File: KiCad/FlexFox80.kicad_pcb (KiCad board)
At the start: 4 copper layers, 111.2 x 80 mm, 169 parts, among them J101 DIN-5_180degree, J102 Conn_01x02, J203 V4, J301 DB9_Female, J302 Conn_01x06, J303 DB9_Male, P203 Power Pole, P301 ISP/PDI, P302 Thru, P304 Header, Q101 LMN200B02, Q102 IRF610, Q201 MUN5213DW1, Q202 DMP4025LSD, Q203 RJK0354DSP, Q301 PN2222A, SW301 SPST, U107 LM5134B, U201 DAC081C085, U202 OPA171, U203 LTC3600, U204 MIC2196, U301 DS3231, U302 ATmega1284P-AU, U303 LP2992, U304 SI5351A, U305 74HC1G08, U306 LP2992, U307 SN74CB3Q3305, U308 LP2992, X301 ASTX-H11-25.MHZ, Y301 20 MHz

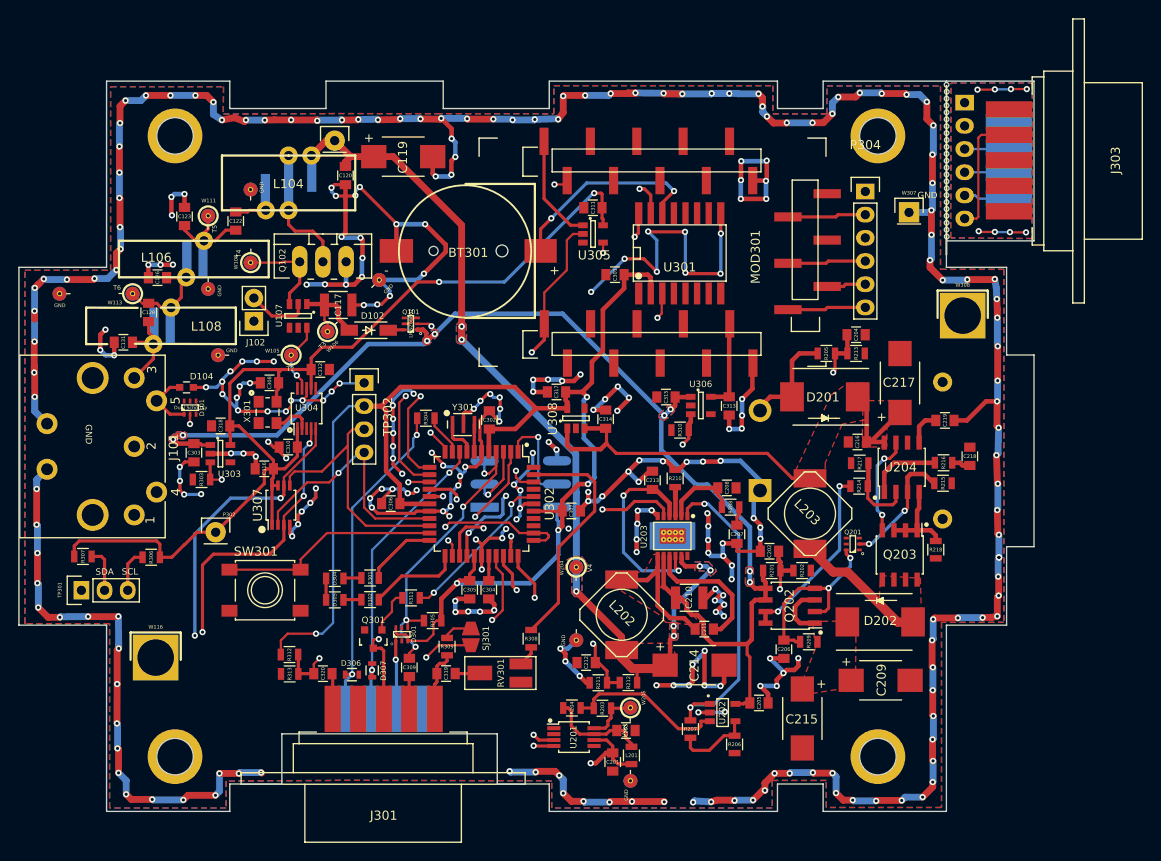
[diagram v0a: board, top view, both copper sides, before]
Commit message: Updates for AVR128DA48
o Board changes
o Gerbers updated
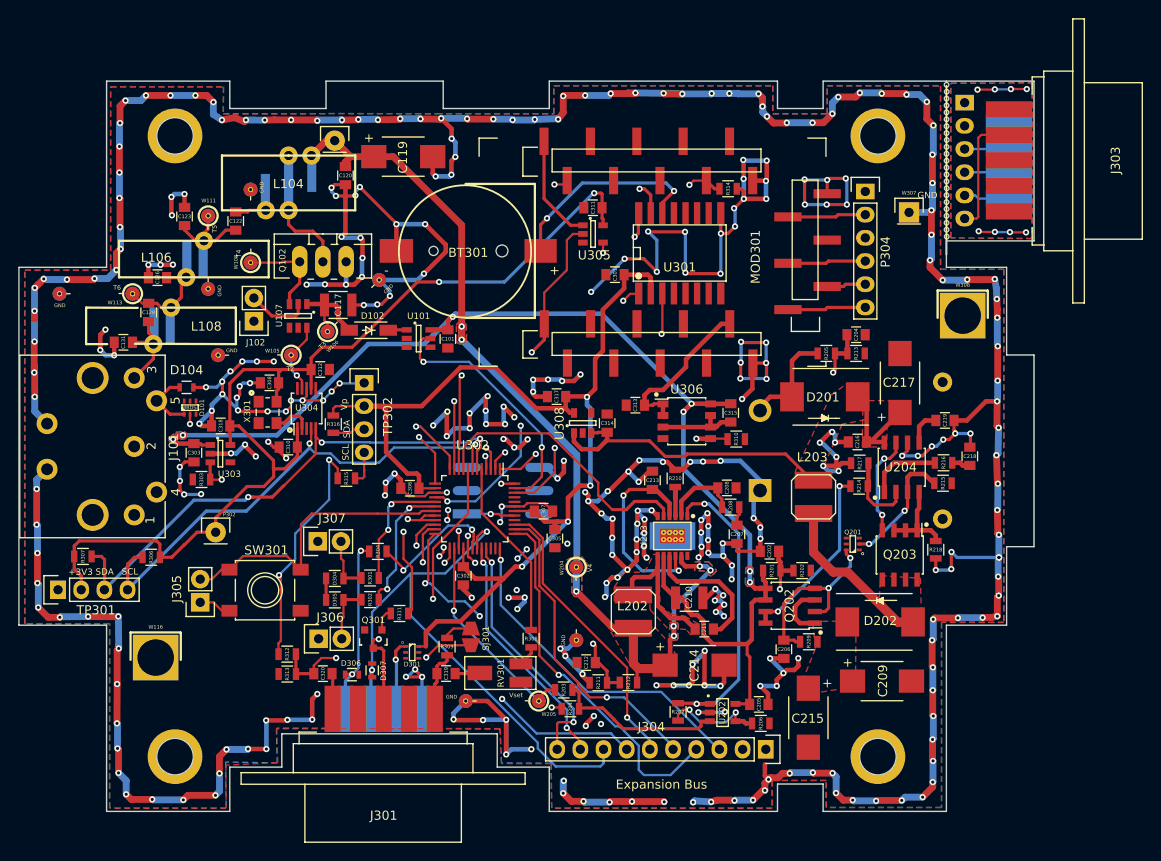
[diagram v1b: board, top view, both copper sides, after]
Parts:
- removed C201, C203, C304: 10uF, Capacitors_SMD:C_0805
- removed C309, C316: 100nF, Capacitors_SMD:C_0805
- removed L201: 10uH, Resistors_SMD:R_0805
- removed Q101: LMN200B02, TO_SOT_Packages_SMD:SOT-363-0.65
- removed R305: 10k, Resistors_SMD:R_0805
- removed U201: DAC081C085, Housings_SSOP:MSOP-8_3x3mm_Pitch0.65mm
- removed U307: SN74CB3Q3305, Housings_SSOP:TSSOP-8_3x3mm_Pitch0.65mm
- removed Y301: 20 MHz, Crystals:CSTNE20M0V53Z000R0
- added C101: 10uF, Capacitors_SMD:C_0805, F.Cu at (63.2, 58.2)
- added J304: Conn_01x10, Pin_Headers:Pin_Header_Straight_1x10, F.Cu at (98.0, 103.2)
- added J305: Conn_01x02, Pin_Headers:Pin_Header_Straight_1x02, F.Cu at (36.1, 87.1)
- added J306: Conn_01x02, Pin_Headers:Pin_Header_Straight_1x02, F.Cu at (49.0, 91.1)
- added J307: Conn_01x02, Pin_Headers:Pin_Header_Straight_1x02, F.Cu at (48.9, 80.4)
- added R314: 560k, Resistors_SMD:R_0805, F.Cu at (93.9, 41.8)
- added R315: 10k, Resistors_SMD:R_0805, F.Cu at (52.1, 73.5)
- added R316: 10k, Resistors_SMD:R_0805, F.Cu at (50.6, 67.6)
- added U101: TPS22810DBVT, TO_SOT_Packages_SMD:SOT-23-6, F.Cu at (60.0, 58.2)
- D101: value Dual Schottky -> MBD54
- D104: value 5V -> ESD; footprint Capacitors_SMD:C_0603 -> Resistors_SMD:R_0603
- D301: value MBD54DWT1GOSCT-ND -> MBD54
- L202, L203: footprint Inductors:CDR7D28MN -> Inductors:2020
- R204: value 536k -> 392k
- R206: value 46.4k -> 27k
- TP301: footprint Pin_Headers:Pin_Header_Straight_1x03 -> Pin_Headers:Pin_Header_Straight_1x04
- U302: value ATmega1284P-AU -> AVR128DA48; footprint Housings_QFP:TQFP-44_10x10mm_Pitch0.8mm -> Housings_QFP:TQFP-48_7x7mm_Pitch0.5mm
- U303, U308: value LP2992 -> LD2985BM33R
- U306: value LP2992 -> LT1763CS8-5; footprint TO_SOT_Packages_SMD:SOT-23-5 -> Housings_SOIC:SOIC-8_3.9x4.9mm_Pitch1.27mm
- X301: value ASTX-H11-25.MHZ -> 25.MHZ TCXO
- moved C302 17.3 mm to (64.9, 84.2), turned to 90 degrees
- moved R304 15.5 mm to (55.5, 81.5)
- moved C305 10.9 mm to (74.9, 80.1)
- moved C313 10.3 mm to (83.7, 65.5), turned to 0 degrees
- moved W205 10.1 mm to (73.2, 97.9), turned to 180 degrees
- moved C315 7.31 mm to (94.2, 66.3), turned to 90 degrees
- moved R310 6.23 mm to (94.8, 69.2), turned to 0 degrees
- moved R203 4.69 mm to (75.9, 96.7), turned to 180 degrees
- moved R206 3.68 mm to (97.5, 100.4), turned to 0 degrees
- moved C307 3.05 mm to (73.7, 77.1)
- moved C306 2.69 mm to (59.0, 74.6)
- moved TP301 2.56 mm to (20.5, 85.7)
- moved U306 2.32 mm to (89.4, 67.3)
- moved R207 2.31 mm to (88.4, 99.1)
- moved D301 2.28 mm to (59.3, 92.6), turned to 270 degrees
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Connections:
- net /Digital/RXD1 renamed WIFI_TX
- D301 pad 3: Vproc -> (no net)
- D301 pad 4: ~RESET~ -> (no net)
- MOD301 pad 13: Net-(MOD301-Pad13) -> /Digital/ADC7
- MOD301 pad 19: DI_TXD0 -> WIFI_RX
- P301 pad 1: MISO -> Net-(P301-Pad1)
- P301 pad 3: SCK -> Net-(P301-Pad3)
- P301 pad 4: MOSI -> Net-(P301-Pad4)
- P301 pad 5: ~RESET~ -> Net-(P301-Pad5)
- R203 pad 2: Net-(R203-Pad2) -> DAC_OUTPUT
- R204 pad 1: Net-(C203-Pad2) -> +3V3_L8
- R301 pad 2: /Digital/PC3 -> /Digital/PC5
- R302 pad 2: /Digital/PC4 -> /Digital/PC6
- R304 pad 1: /Digital/TXD0 -> /Digital/TXD4
- R306 pad 2: DI_SCL -> /Digital/SCL1
- R307 pad 2: DI_SDA -> /Digital/SDA1
- SW301 pad 1: /Digital/PC2 -> /Digital/PC7
- TP301 pad 2: DI_SDA -> +3V3_L8
- TP301 pad 3: DI_SCL -> /Digital/SDA1
- U301 pad 1: Net-(U301-Pad1) -> 32KHZ_SQUAREWAVE
- U302 pad 1: MOSI -> WIFI_ENABLE
- U302 pad 10: /Digital/TXD0 -> WIFI_RX
- U302 pad 12: DI_TXD0 -> RTC_SDA
- U302 pad 13: HF_ENABLE -> RTC_SCL
- U302 pad 14: 3V3_PWR_ENABLE -> Vproc
- U302 pad 15: MAIN_PWR_ENABLE -> GND
- U302 pad 16: TX_FINAL_VOLTAGE_ENABLE -> 32KHZ_SQUAREWAVE
- U302 pad 17: Vproc -> /Digital/PC5
- U302 pad 18: GND -> /Digital/PC6
- U302 pad 19: RTC_SCL -> /Digital/PC7
- U302 pad 2: MISO -> ~WIFI_RESET~
- U302 pad 20: RTC_SDA -> 80M_ANTENNA_DETECT
- U302 pad 21: /Digital/PC2 -> 80M_ANTENNA_DETECT
- U302 pad 22: /Digital/PC3 -> PROC_HT_AUDIO_IN
- U302 pad 23: /Digital/PC4 -> TX_BATTERY_VOLTAGE
- U302 pad 24: ~ANT_CONNECT_INT~ -> TX_+12_VOLTAGE
- U302 pad 25: WIFI_ENABLE -> TX_PA_VOLTAGE
- U302 pad 26: ~WIFI_RESET~ -> DAC_OUTPUT
- U302 pad 27: Vproc -> /Digital/ADC7
- U302 pad 28: GND -> Vproc
- U302 pad 29: Net-(C304-Pad2) -> GND
- U302 pad 3: SCK -> 3V3_PWR_ENABLE
- U302 pad 30: PROC_HT_AUDIO_IN -> /Digital/TXD4
- U302 pad 31: TX_PA_VOLTAGE -> RXD_TO_FTDI
- U302 pad 32: TX_BATTERY_VOLTAGE -> /Digital/PE2
- U302 pad 33: TX_+12_VOLTAGE -> /Digital/PE3
- U302 pad 34: 80M_ANTENNA_DETECT -> Net-(U302-Pad34)
- U302 pad 35: 80M_ANTENNA_DETECT -> Net-(U302-Pad35)
- U302 pad 36: /Digital/PA1 -> /Digital/PF2
- U302 pad 37: /Digital/PA0 -> /Digital/PF3
- U302 pad 38: Vproc -> /Digital/PF4
- U302 pad 39: GND -> /Digital/PF5
- U302 pad 4: ~RESET~ -> PROC_PTT_OUT
- U302 pad 40: PROC_PTT_OUT -> /Digital/PF6
- U302 pad 41: /Digital/PB1 -> Net-(P301-Pad1)
- U302 pad 42: RTC_SQW -> Vproc
- U302 pad 43: PROC_TONE_OUT -> GND
- U302 pad 44: /Digital/PB4 -> /Digital/PA0
- U302 pad 5: Vproc -> PROC_TONE_OUT
- U302 pad 6: GND -> /Digital/SDA1
- U302 pad 7: Net-(U302-Pad7) -> /Digital/SCL1
- U302 pad 8: Net-(U302-Pad8) -> MAIN_PWR_ENABLE
- U302 pad 9: RXD_TO_FTDI -> TX_FINAL_VOLTAGE_ENABLE
- U304 pad 4: DI_SCL -> /Digital/SCL1
- U304 pad 5: DI_SDA -> /Digital/SDA1
- U306 pad 1: +12V -> Net-(C313-Pad2)
- U306 pad 2: GND -> Net-(C313-Pad2)
- U306 pad 3: WIFI_ENABLE -> GND
- U306 pad 5: Net-(C313-Pad2) -> WIFI_ENABLE
- W205 pad 1: Net-(R203-Pad2) -> DAC_OUTPUT
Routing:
- net GND: track 793.7 -> 930.0 mm, vias 314 -> 353
- net DI_SDA: track 97.8 -> 0.00 mm, vias 3 -> 0
- net DI_SCL: track 93.5 -> 0.00 mm, vias 4 -> 0
- net /Digital/SDA1: track 0.00 -> 59.0 mm, vias 0 -> 3
- net /Digital/SCL1: track 0.00 -> 55.8 mm, vias 0 -> 2
- net /Digital/ADC7: track 0.00 -> 54.9 mm, vias 0 -> 2
- net /Digital/TXD4: track 0.00 -> 49.3 mm, vias 0 -> 3
- net DI_TXD0: track 40.9 -> 0.00 mm, vias 2 -> 0
- net /Digital/PF3: track 0.00 -> 40.6 mm, vias 0 -> 1
- net WIFI_RX: track 0.00 -> 37.1 mm, vias 0 -> 2
- net /Digital/PF2: track 0.00 -> 36.8 mm, vias 0 -> 1
- net 32KHZ_SQUAREWAVE: track 0.00 -> 35.7 mm, vias 0 -> 3
- net ~RESET~: track 35.4 -> 0.00 mm, vias 4 -> 0
- net /Digital/PF4: track 0.00 -> 34.4 mm, vias 0 -> 1
- net /Digital/PC7: track 0.00 -> 33.0 mm
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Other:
- outline, holes or cut-outs redrawn
- board text added: "+3V3"
- board text added: "Expansion Bus"
- board text added: "FlexFox80 Version 2.0 - Jan 2022"
- board text added: "N/C"
- board text added: "UPDI"
- board text added: "Vp"
- board text removed: "FlexFox80 Version P1.0 - May 2021"
- board text removed: "MISO"
- board text removed: "MOSI"
- board text removed: "RESET"
- board text removed: "SCK"

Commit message: Updates
o Added fan control
o Fixed pinout for load switch device
o Updated gerbers
o Updated BOM
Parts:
- added C304: 10uF, Capacitors_SMD:C_0805, F.Cu at (33.8, 97.1)
- added J308: Conn_01x02, Pin_Headers:Pin_Header_Straight_1x02, F.Cu at (38.0, 99.3)
- added U307: TPS22810DBVT, TO_SOT_Packages_SMD:SOT-23-6, F.Cu at (37.5, 93.9)
- moved C101 1.17 mm to (63.3, 59.4)
- moved U101 0.78 mm to (60.0, 57.4), turned to 180 degrees
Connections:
- U101 pad 1: Net-(D102-Pad1) -> +12V
- U101 pad 2: Net-(U101-Pad2) -> GND
- U101 pad 3: Net-(U101-Pad3) -> FET_DRIVER_ENABLE
- U101 pad 4: GND -> Net-(U101-Pad4)
- U101 pad 5: FET_DRIVER_ENABLE -> Net-(U101-Pad5)
- U101 pad 6: +12V -> Net-(D102-Pad1)
- U302 pad 45: /Digital/PA1 -> FAN_ENABLE
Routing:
- net FAN_ENABLE: track 0.00 -> 58.3 mm, vias 0 -> 2
- net Net-(C304-Pad1): track 0.00 -> 8.53 mm
- net Net-(J308-Pad2): track 0.00 -> 5.97 mm
- net +3V3_L8: track 193.3 -> 190.8 mm
- net FET_DRIVER_ENABLE: track 28.0 -> 29.9 mm
- net +12V: track 141.7 -> 142.9 mm
- net GND: track 930.0 -> 928.9 mm, vias 353 -> 351
- net Net-(D102-Pad1): track 2.11 -> 3.10 mm
- net ~WIFI_RESET~: track 31.3 -> 30.4 mm
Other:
- board text added: "FAN"
- board text added: "Vin"
- board text added: "Vout"

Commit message: Fan Control Update
o Corrected an error in the fan control circuit
o Updated all gerbers and fab files
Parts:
- added JP301: Jumper_NO_Small, Wire_Connections_Bridges:Solder-Jumper-NO-SMD-Pad_Small, F.Cu at (41.7, 91.4)
- moved C304 7.88 mm to (41.7, 96.5), turned to 0 degrees
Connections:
- J308 pad 1: Net-(C304-Pad1) -> Net-(J308-Pad1)
- J308 pad 2: Net-(J308-Pad2) -> Net-(C304-Pad1)
- U307 pad 1: Net-(J308-Pad2) -> Net-(C304-Pad1)
- U307 pad 6: Net-(C304-Pad1) -> Net-(J308-Pad1)
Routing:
- net +12V: track 142.9 -> 175.0 mm, vias 7 -> 9
- net GND: track 928.9 -> 947.6 mm, vias 351 -> 359
- net Net-(J308-Pad2): track 5.97 -> 0.00 mm
- net Net-(J308-Pad1): track 0.00 -> 5.24 mm
- net Net-(C304-Pad1): track 8.53 -> 10.5 mm

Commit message: Updated PCB
o Changed U302 footprint to more closely match 48-TQFP (7x7) shown in the AVR128DA48 datasheet
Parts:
- U302: footprint Housings_QFP:TQFP-48_7x7mm_Pitch0.5mm -> Housings_QFP:TQFP-48_7x7mm_Pitch0.5mm_AVR128DA48
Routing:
- net Vproc: track 182.6 -> 183.3 mm

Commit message: Gerber Update
Removed flood fills of U302 ground pins.
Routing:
- net GND: track 947.1 -> 956.4 mm, vias 359 -> 362

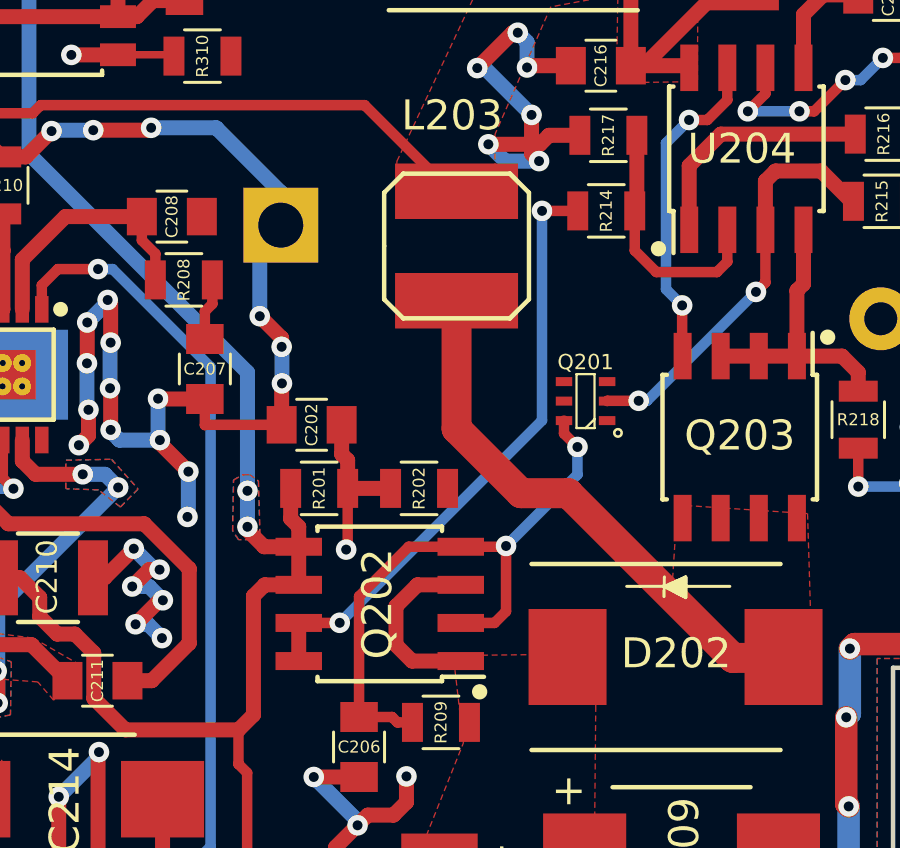
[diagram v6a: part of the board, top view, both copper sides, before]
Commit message: Gerber Update
o Added J201 to optionally bypass U204
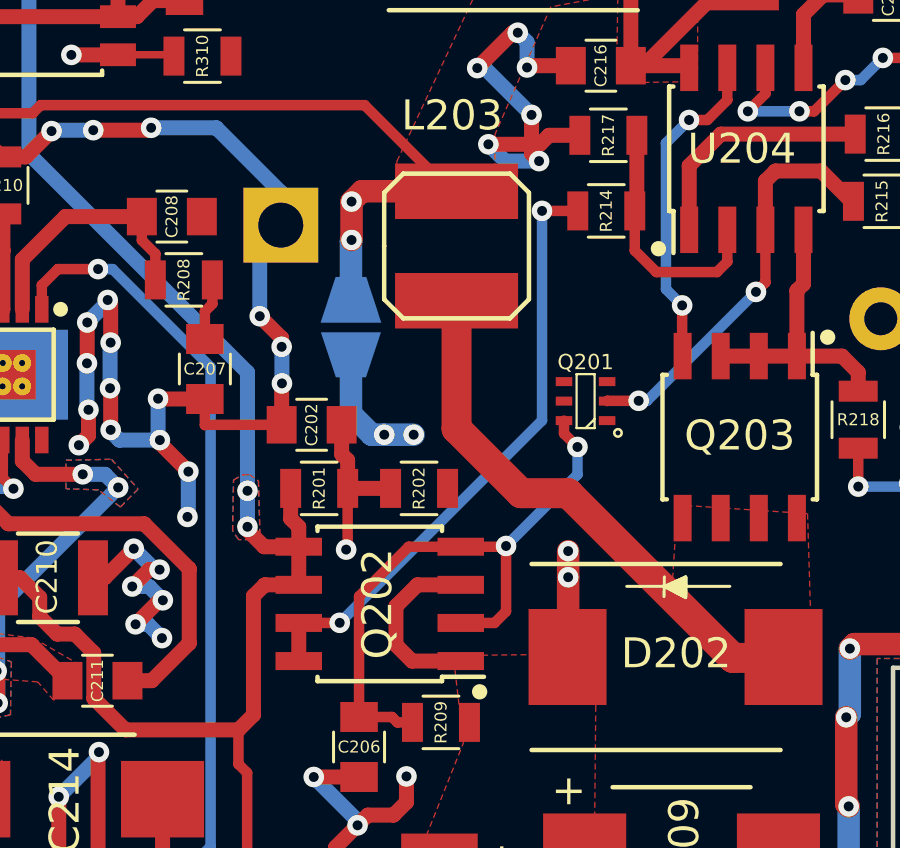
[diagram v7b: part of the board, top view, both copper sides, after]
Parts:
- added JP201: Boost Bypass, Wire_Connections_Bridges:Solder-Jumper-NO-SMD-Pad_Small, B.Cu at (99.7, 78.2)
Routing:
- net Net-(C209-Pad1): track 6.13 -> 22.6 mm, vias 0 -> 4
- net EXTERNAL_3.6V-15V_SUPPLY: track 44.7 -> 51.7 mm, vias 0 -> 2

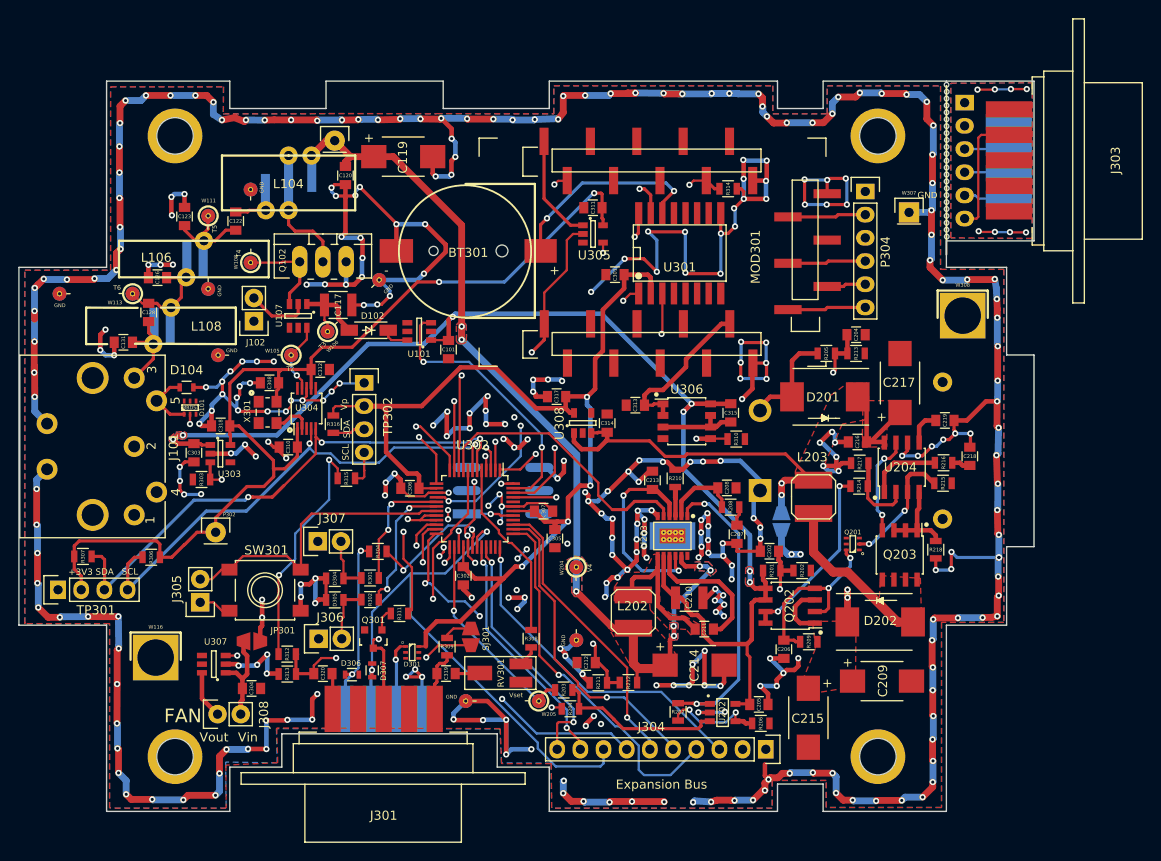
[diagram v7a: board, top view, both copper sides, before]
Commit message: Gerber Updates
o Changed parts for C128, L203 and L204 to help with parts shortages
o Updated footprints
o Updated schematic
o Updated BOM
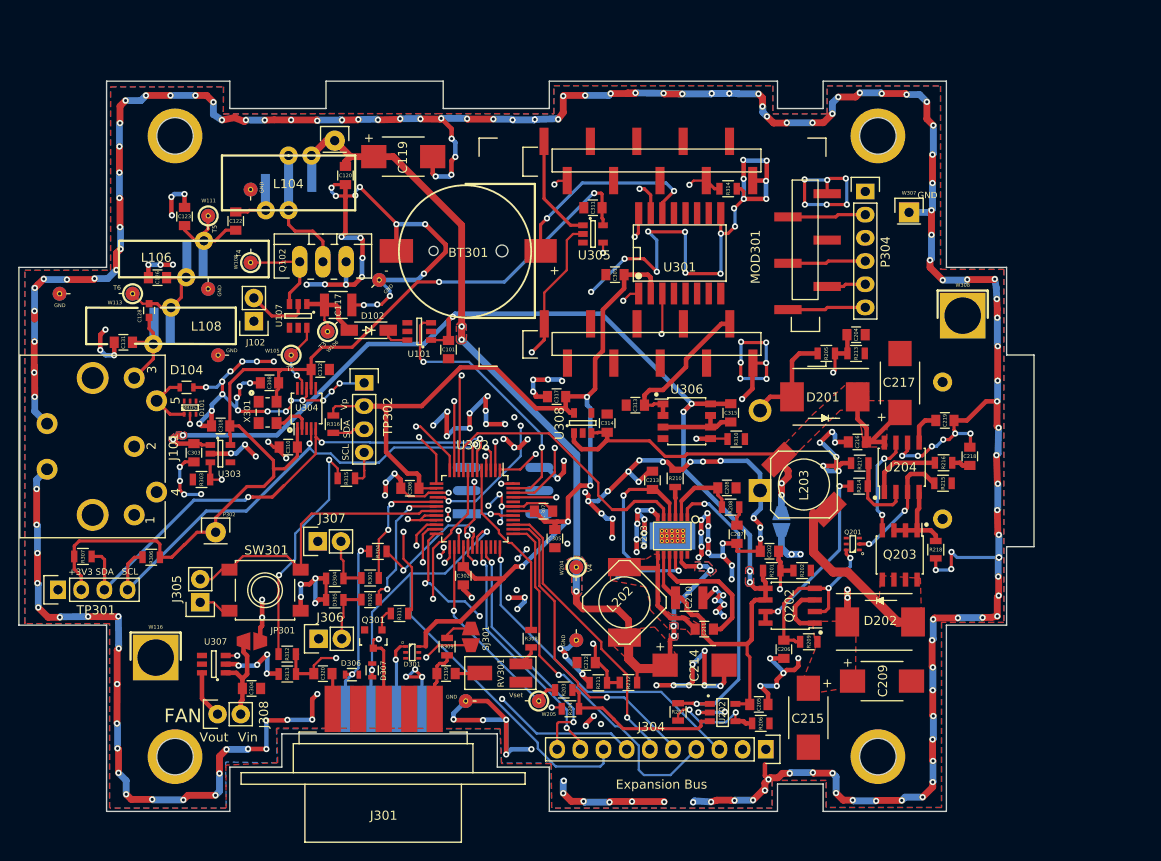
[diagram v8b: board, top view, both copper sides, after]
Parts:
- removed ? (x23): NP_Thru_Hole_0.5mm, Mounting_Holes:NP_Thru_Hole_0.5mm
- removed J302: Conn_01x06, Pin_Headers:Pin_Header_Angled_1x06
- removed J303: DB9_Male, Connect:DB9F_CI
- C128: footprint Capacitors_SMD:C_0805 -> Capacitors_SMD:C_0603
- L202, L203: footprint Inductors:2020 -> Inductors:CDR7D28MN
- moved L203 1.71 mm to (102.2, 74.2), turned to 180 degrees
- moved L202 1.41 mm to (82.5, 87.1), turned to 315 degrees
- moved C128 0.22 mm to (30.5, 55.1)
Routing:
- net GND1: track 29.9 -> 0.00 mm, vias 8 -> 0
- net Net-(J302-Pad6): track 13.7 -> 0.00 mm
- net GND: track 956.4 -> 946.0 mm, vias 362 -> 356
- net Net-(J302-Pad5): track 5.01 -> 0.00 mm
- net Net-(J302-Pad3): track 4.93 -> 0.00 mm
- net Net-(J302-Pad4): track 4.90 -> 0.00 mm
- net EXTERNAL_3.6V-15V_SUPPLY: track 51.7 -> 47.6 mm
- net Net-(C211-Pad1): track 15.8 -> 13.9 mm
- net +2to+12V: track 103.3 -> 104.2 mm
- removed copper zone on B.Cu, net GND1
- removed copper zone on F.Cu, net GND1
- removed copper zone on In1.Cu, net GND1
- removed copper zone on In2.Cu, net GND1
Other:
- outline, holes or cut-outs redrawn
